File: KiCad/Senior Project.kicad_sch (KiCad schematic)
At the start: 29 parts, among them J1 USB_C_Receptacle_USB2.0_16P, J2 Screw_Terminal_01x02, J3 Screw_Terminal_01x06, SW1 SW_Push, SW2 SW_Push, U1 ESP32-S3FH4R2, X1 FC-135 32.7680KA-A5, Y2 Crystal_GND23

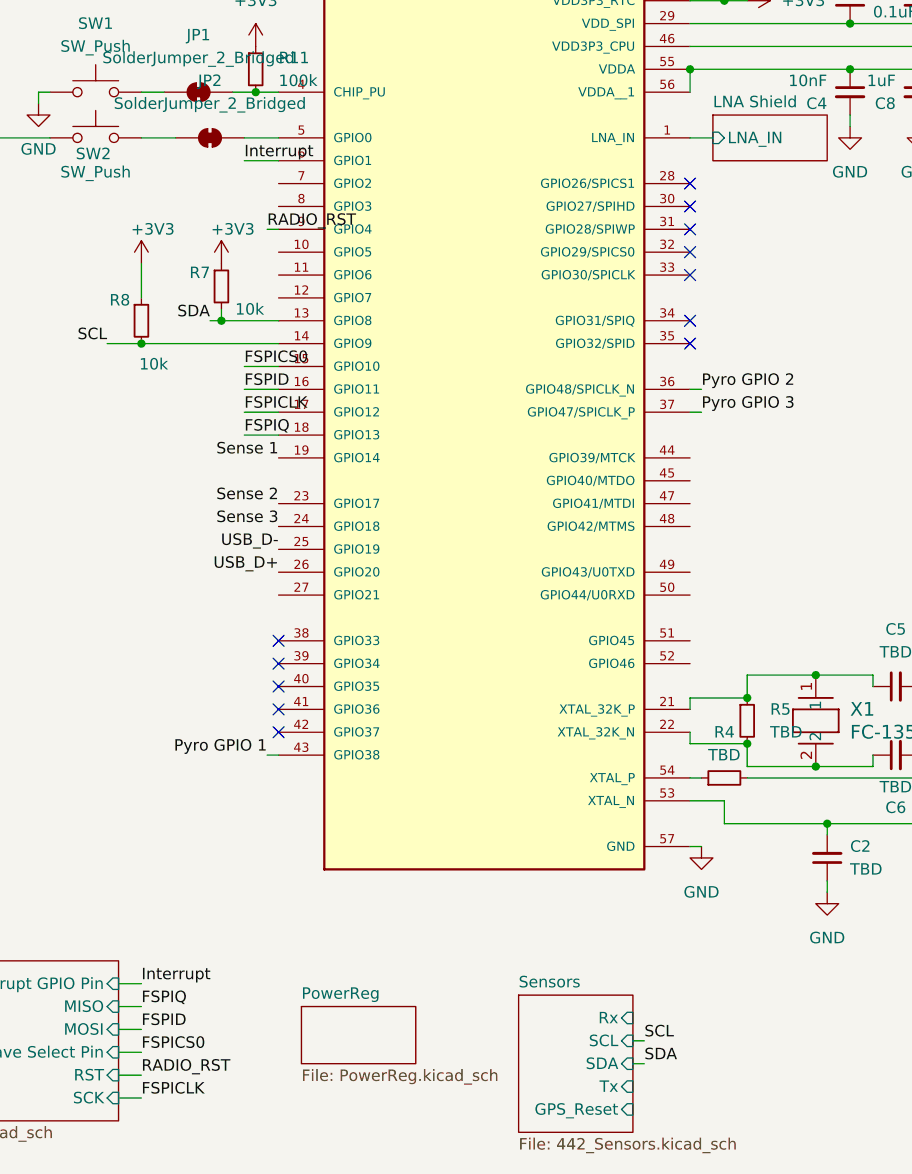
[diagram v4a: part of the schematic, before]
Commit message: Routing, schematic fixes, and minor placement changes.
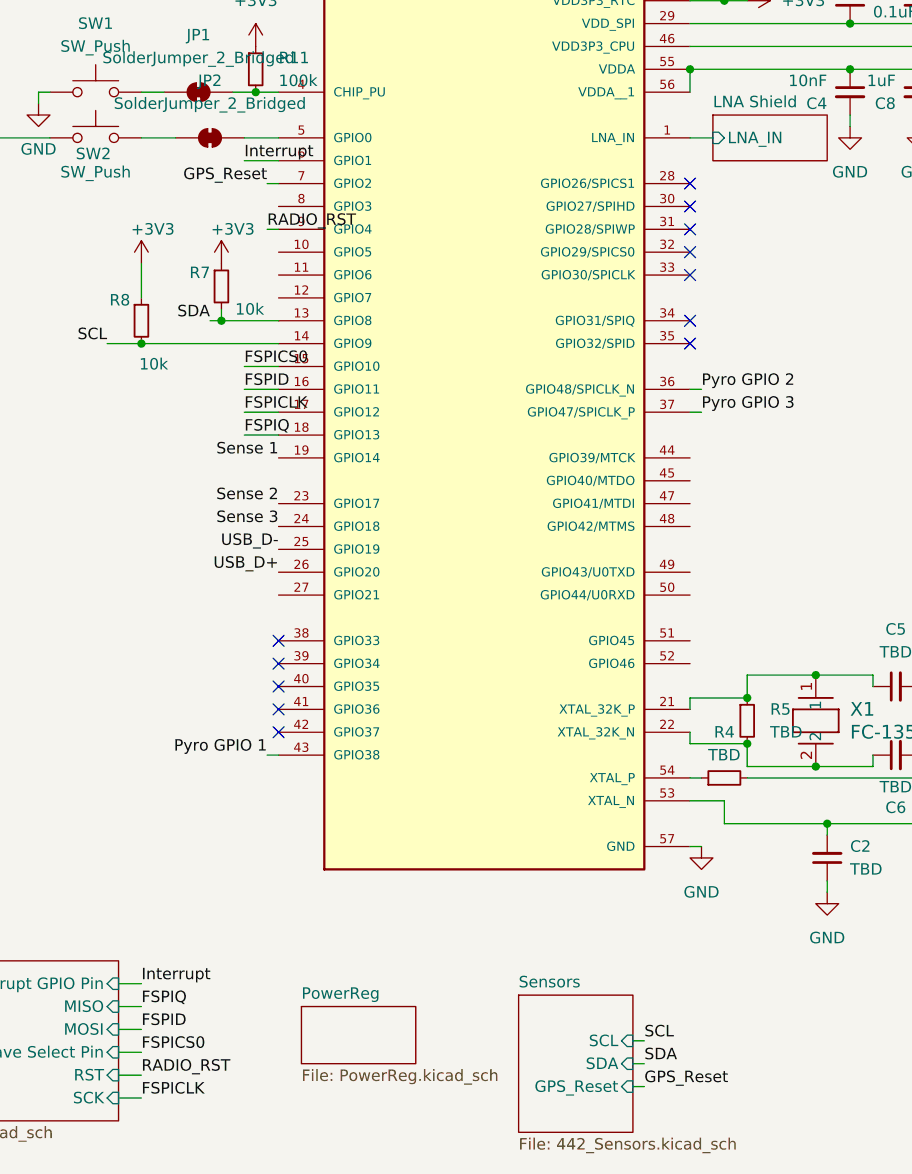
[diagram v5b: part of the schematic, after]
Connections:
- net GPS_Reset: now reaches U1.7 (GPIO2)
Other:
- sheet Sensors ports: added none; removed Rx, Tx
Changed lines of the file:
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@@
 	(wire
 		(pts
+			(xy 119.38 72.39) (xy 120.65 72.39)
+		)
+		(stroke
+			(width 0)
+			(type default)
+		)
+	)
+	(wire
+		(pts
 			(xy 102.87 168.91) (xy 105.41 168.91)
 		)
@@
 	(wire
 		(pts
+			(xy 160.02 172.72) (xy 161.29 172.72)
+		)
+		(stroke
+			(width 0)
+			(type default)
+		)
+	)
+	(wire
+		(pts
 			(xy 207.01 138.43) (xy 212.09 138.43)
 		)
@@
 		)
 	)
+	(label "GPS_Reset"
+		(at 119.38 72.39 180)
+		(effects
+			(font
+				(size 1.27 1.27)
+			)
+			(justify right bottom)
+		)
+	)
 	(label "Pyro GPIO 1"
 		(at 119.38 135.89 180)
@@
 		)
 	)
+	(label "GPS_Reset"
+		(at 161.29 172.72 0)
+		(effects
+			(font
+				(size 1.27 1.27)
+			)
+			(justify left bottom)
+		)
+	)
 	(label "Sense 2"
 		(at 120.65 107.95 180)
@@
 			)
 		)
-		(pin "Rx" input
-			(at 160.02 165.1 0)
-			(effects
-				(font
-					(size 1.27 1.27)
-				)
-				(justify right)
-			)
-		)
 		(pin "SCL" input
 			(at 160.02 167.64 0)
@@
 			)
 		)
-		(pin "Tx" input
-			(at 160.02 172.72 0)
-			(effects
-				(font
-					(size 1.27 1.27)
-				)
-				(justify right)
-			)
-		)
 		(pin "GPS_Reset" input
-			(at 160.02 175.26 0)
+			(at 160.02 172.72 0)
 			(effects
 				(font

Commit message: a
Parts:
- removed D1: D_Schottky, symbol Device:D_Schottky
- added D1: D, symbol Device:D
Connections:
- net +BATT: now also D1.1 (K)
- net at J1.A4 (VBUS), J1.A9 (VBUS), J1.B4 (VBUS)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: now also D1.2 (A)
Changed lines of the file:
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@@
 	)
 	(symbol
-		(lib_id "Device:D_Schottky")
-		(at 69.85 44.45 90)
+		(lib_id "Device:D")
+		(at 69.85 44.45 270)
 		(unit 1)
 		(exclude_from_sim no)
@@
 		(fields_autoplaced yes)
 		(property "Reference" "D1"
-			(at 72.39 43.4974 90)
+			(at 72.39 43.1799 90)
 			(effects
 				(font
 					(size 1.27 1.27)
 				)
-				(justify right)
+				(justify left)
 			)
 		)
-		(property "Value" "D_Schottky"
-			(at 72.39 46.0374 90)
+		(property "Value" "D"
+			(at 72.39 45.7199 90)
 			(effects
 				(font
 					(size 1.27 1.27)
 				)
-				(justify right)
+				(justify left)
 			)
 		)
@@
 			)
 		)
-		(property "Description" "Schottky diode"
+		(property "Description" "Diode"
 			(at 69.85 44.45 0)
 			(effects
@@
 			)
 		)
-		(pin "1"
+		(property "Sim.Device" "D"
+			(at 69.85 44.45 0)
+			(effects
+				(font
+					(size 1.27 1.27)
+				)
+				(hide yes)
+			)
+		)
+		(property "Sim.Pins" "1=K 2=A"
+			(at 69.85 44.45 0)
+			(effects
+				(font
+					(size 1.27 1.27)
+				)
+				(hide yes)
+			)
 		)
 		(pin "2"
 		)
+		(pin "1"
+		)
 		(instances

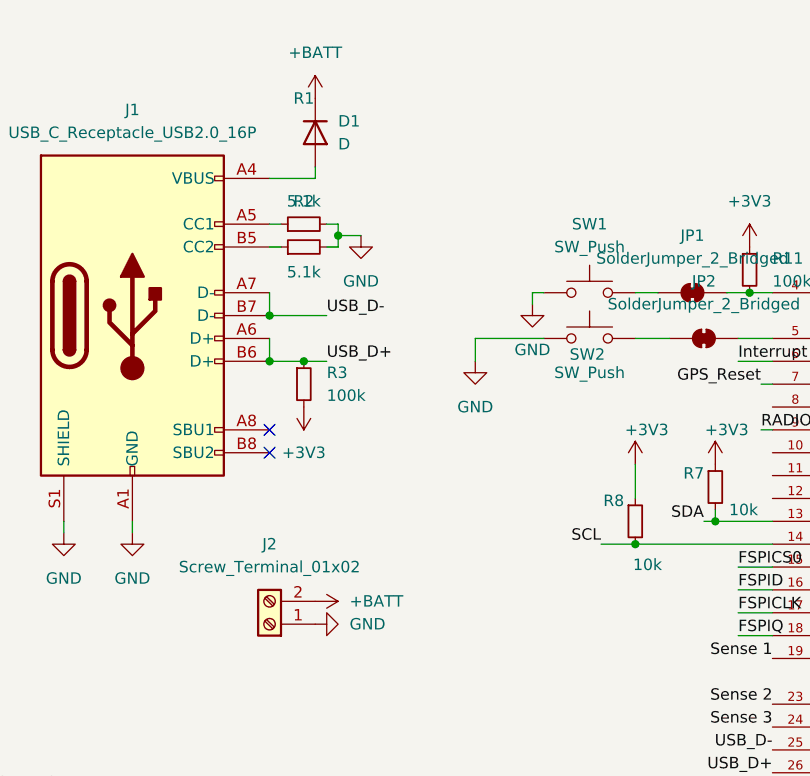
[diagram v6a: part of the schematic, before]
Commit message: Did some symbol changes, need to add more
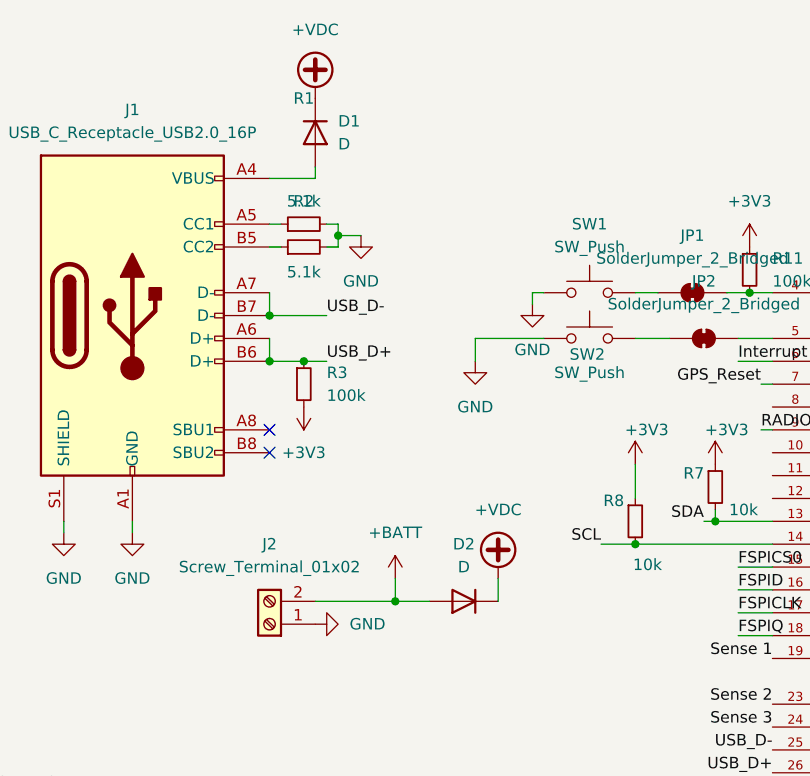
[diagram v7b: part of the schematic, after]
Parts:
- added D2: D, VS_10BQ015HM3_5BT:CR_SMBDO-214AA_VIS, symbol Device:D
- D1: footprint (none) -> VS_10BQ015HM3_5BT:CR_SMBDO-214AA_VIS
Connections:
- net +BATT: now also D2.2 (A); no longer D1.1 (K)
- new net +VDC: D1.1 (K), D2.1 (K)

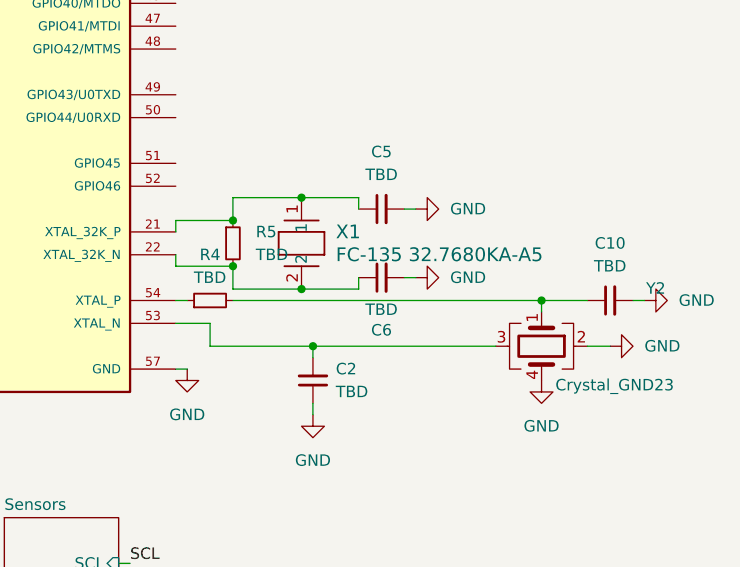
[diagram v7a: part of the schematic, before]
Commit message: Added Diodes and did some routing
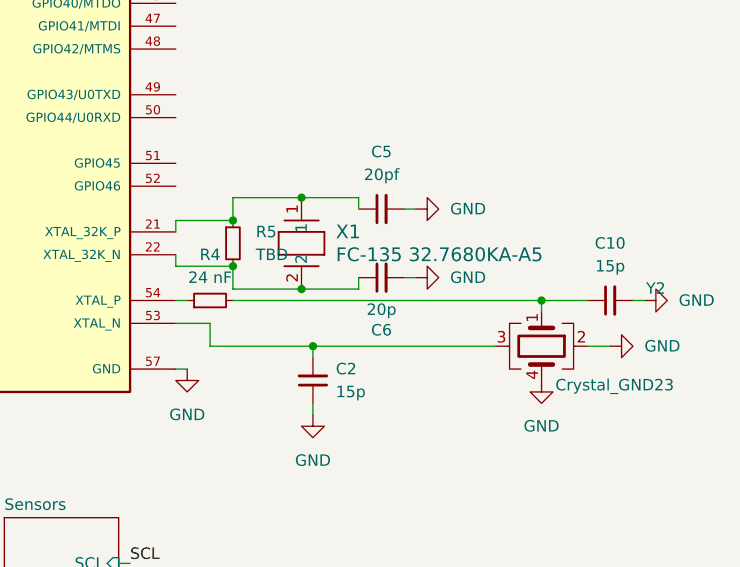
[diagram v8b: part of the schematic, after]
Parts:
- C10, C2: value TBD -> 15p
- C5: value TBD -> 20pf
- C6: value TBD -> 20p
- R4: value TBD -> 24 nF
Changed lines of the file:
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@@
 			)
 		)
-		(property "Value" "TBD"
+		(property "Value" "20p"
 			(at 189.23 139.446 90)
 			(effects
@@
 			)
 		)
-		(property "Value" "TBD"
+		(property "Value" "15p"
 			(at 214.6363 134.62 90)
 			(effects
@@
 			)
 		)
-		(property "Value" "TBD"
+		(property "Value" "24 nF"
 			(at 170.18 135.89 90)
 			(effects
@@
 			)
 		)
-		(property "Value" "TBD"
+		(property "Value" "20pf"
 			(at 189.2363 124.46 90)
 			(effects
@@
 			)
 		)
-		(property "Value" "TBD"
+		(property "Value" "15p"
 			(at 184.15 148.5835 0)
 			(effects
